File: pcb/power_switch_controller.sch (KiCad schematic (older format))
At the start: 38 parts, among them P1 PWR_JACK_2.5x5.5, P2 HEADER_01X03, P3 BNC_DOUBLE_RA, P4 HEADER_02X08, P5 HEADER_02X08, SW1 SPST_SERIES_M, U1 MAX6817, U2 TLE723X, U3 TLE723X

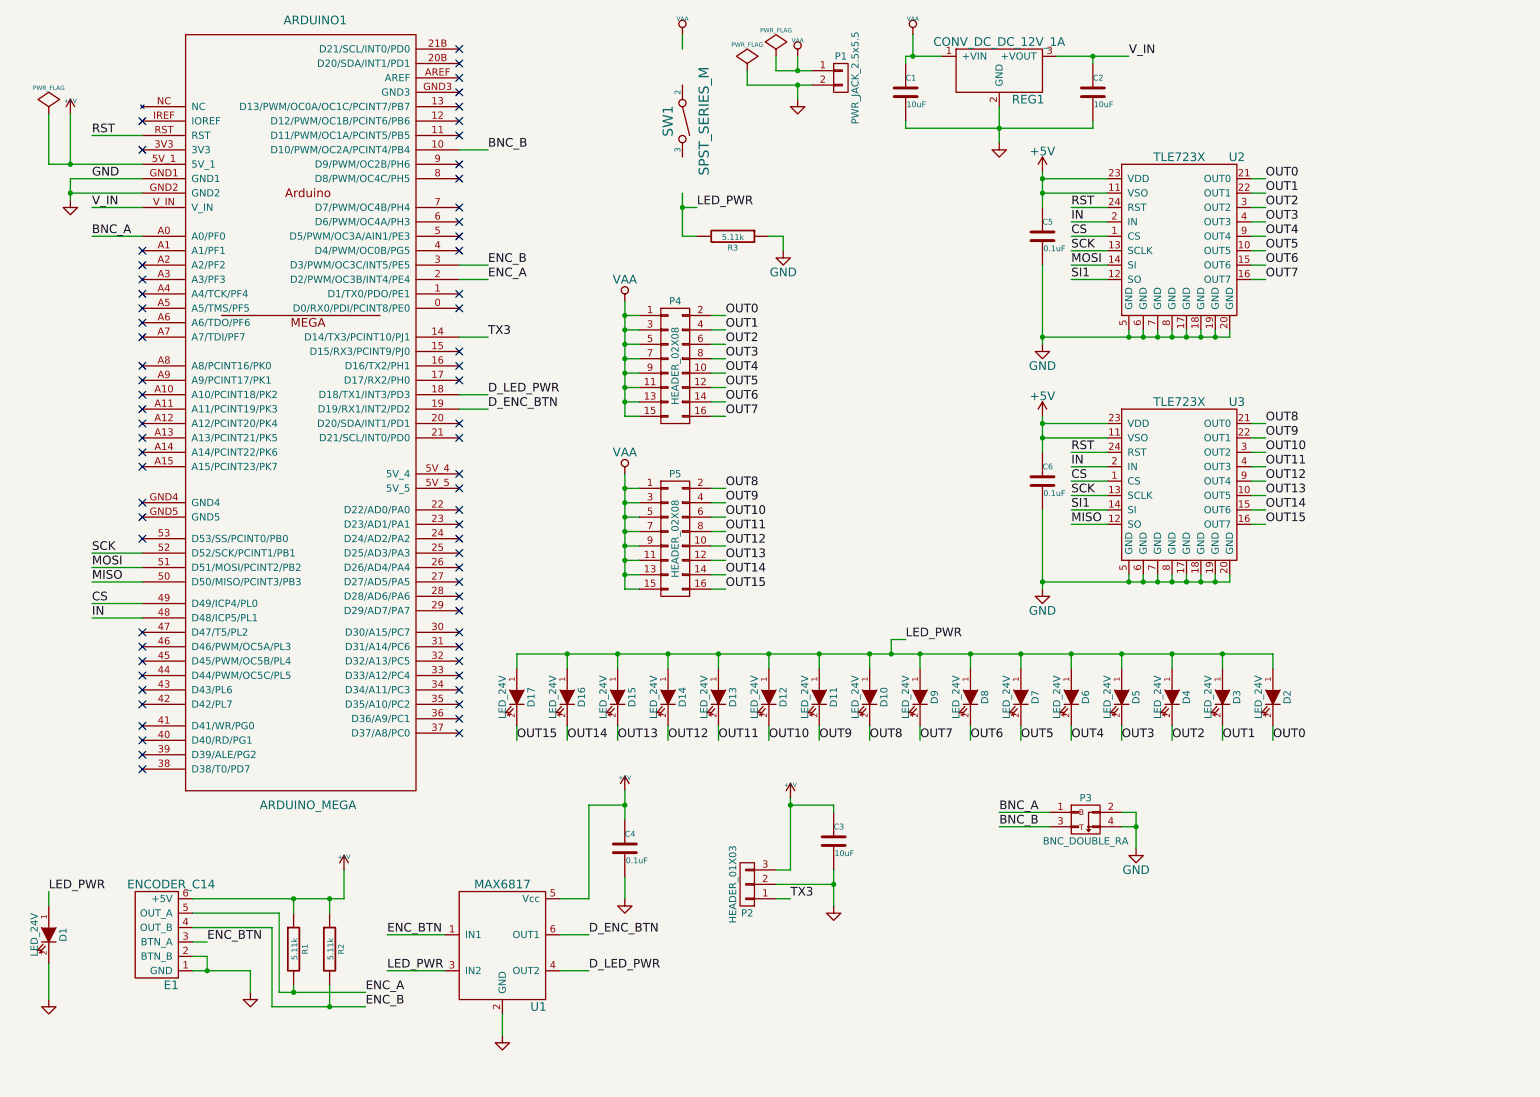
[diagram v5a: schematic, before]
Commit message: Progress towards 32 power switches.
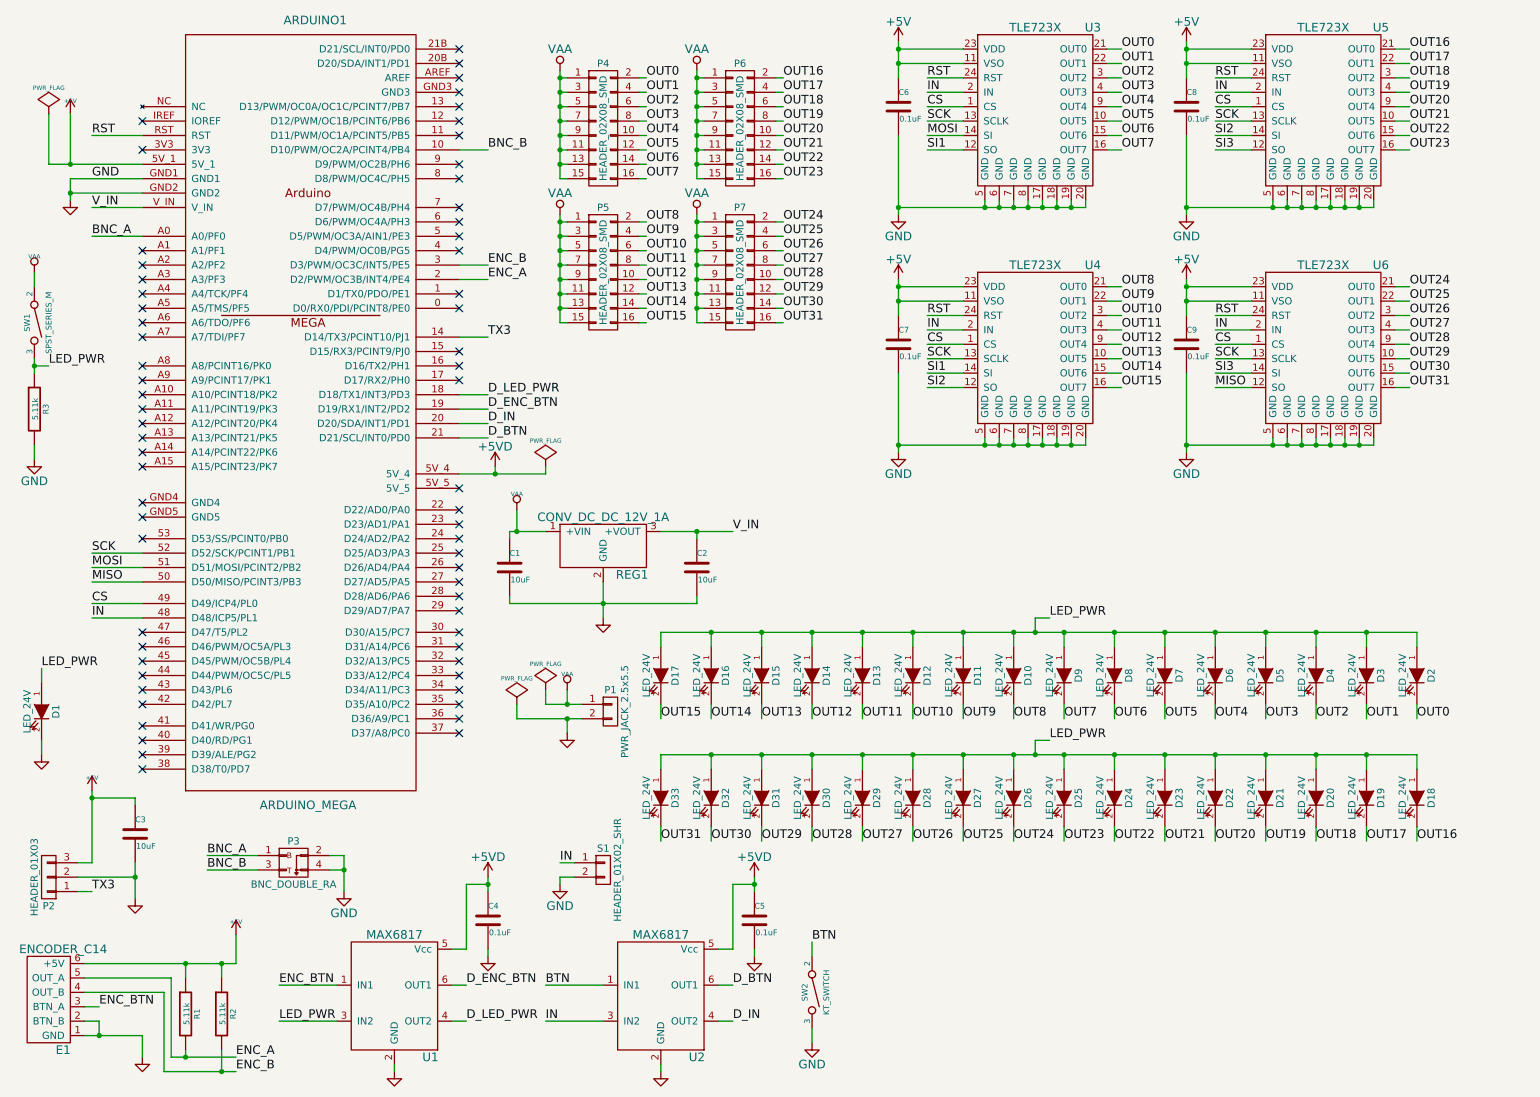
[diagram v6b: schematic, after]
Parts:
- removed P4, P5: HEADER_02X08, power_switch_controller:HEADER_02x08, symbol HEADER_02X08
- added C5, C6, C7: 0.1uF, power_switch_controller:SM1210, symbol 0.1uF
- added D10, D11, D12, D13, D14, D15, D16, D17, D2, D3, D4, D5, D6, D7, D8, D9: LED_24V, power_switch_controller:LED_555-3XXX, symbol LED_24V
- added P4, P5, P6, P7: HEADER_02X08_SMD, power_switch_controller:HEADER_02x08_SMD, symbol HEADER_02X08_SMD
- added S1: HEADER_01X02_SHR, power_switch_controller:Header_Shrouded_2_Pin, symbol HEADER_01X02_SHR
- added SW2: KT_SWITCH, power_switch_controller:KT_SWITCH, symbol KT_SWITCH
- added U2: MAX6817, power_switch_controller:MAX6817, symbol MAX6817
- added U3, U4: TLE723X, power_switch_controller:TLE723X, symbol TLE723X
- P2: footprint power_switch_controller:Header_Shrouded_3_Pin -> footprints:Header_3_Pin
- renumbered C5 to C8, C6 to C9, D2 to D18, D3 to D19, D4 to D20, D5 to D21, D6 to D22, D7 to D23, D8 to D24, D9 to D25, D10 to D26, D11 to D27, D12 to D28, D13 to D29, D14 to D30, D15 to D31, D16 to D32, D17 to D33, U2 to U5, U3 to U6
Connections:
- net +5V: now also C6.1, C7.1, U3.11 (VSO), U3.23 (VDD), U4.11 (VSO), U4.23 (VDD); no longer C4.1, U1.5 (Vcc)
- net CS: now also U3.1 (CS), U4.1 (CS)
- net GND: now also R3.2, C5.2, C6.2, C7.2, S1.2 (P2), SW2.3, U2.2 (GND), U3.17 (GND), U3.18 (GND), U3.19 (GND), U3.20 (GND), U3.5 (GND), U3.6 (GND), U3.7 (GND), U3.8 (GND), U4.17 (GND), U4.18 (GND), U4.19 (GND), U4.20 (GND), U4.5 (GND), U4.6 (GND), U4.7 (GND), U4.8 (GND); no longer R3.1
- net IN: now also S1.1 (P1), U2.3 (IN2), U3.2 (IN), U4.2 (IN)
- net LED_PWR: now also R3.1, SW1.3, D10.1 (A), D11.1 (A), D12.1 (A), D13.1 (A), D14.1 (A), D15.1 (A), D16.1 (A), D17.1 (A), D2.1 (A), D3.1 (A), D4.1 (A), D5.1 (A), D6.1 (A), D7.1 (A), D8.1 (A), D9.1 (A); no longer R3.2
- net MOSI: now also U3.14 (SI); no longer U5.14 (SI)
- net OUT0: now also D2.2 (K), P4.2 (P2), U3.21 (OUT0); no longer D18.2 (K), U5.21 (OUT0)
- net OUT1: now also D3.2 (K), P4.4 (P4), U3.22 (OUT1); no longer D19.2 (K), U5.22 (OUT1)
- net OUT10: now also D12.2 (K), P5.6 (P6), U4.3 (OUT2); no longer D28.2 (K), U6.3 (OUT2)
- net OUT11: now also D13.2 (K), P5.8 (P8), U4.4 (OUT3); no longer D29.2 (K), U6.4 (OUT3)
- net OUT12: now also D14.2 (K), P5.10 (P10), U4.9 (OUT4); no longer D30.2 (K), U6.9 (OUT4)
- net OUT13: now also D15.2 (K), P5.12 (P12), U4.10 (OUT5); no longer D31.2 (K), U6.10 (OUT5)
- net OUT14: now also D16.2 (K), P5.14 (P14), U4.15 (OUT6); no longer D32.2 (K), U6.15 (OUT6)
- net OUT15: now also D17.2 (K), P5.16 (P16), U4.16 (OUT7); no longer D33.2 (K), U6.16 (OUT7)
- net OUT2: now also D4.2 (K), P4.6 (P6), U3.3 (OUT2); no longer D20.2 (K), U5.3 (OUT2)
- net OUT3: now also D5.2 (K), P4.8 (P8), U3.4 (OUT3); no longer D21.2 (K), U5.4 (OUT3)
- net OUT4: now also D6.2 (K), P4.10 (P10), U3.9 (OUT4); no longer D22.2 (K), U5.9 (OUT4)
- net OUT5: now also D7.2 (K), P4.12 (P12), U3.10 (OUT5); no longer D23.2 (K), U5.10 (OUT5)
- net OUT6: now also D8.2 (K), P4.14 (P14), U3.15 (OUT6); no longer D24.2 (K), U5.15 (OUT6)
- net OUT7: now also D9.2 (K), P4.16 (P16), U3.16 (OUT7); no longer D25.2 (K), U5.16 (OUT7)
- net OUT8: now also D10.2 (K), P5.2 (P2), U4.21 (OUT0); no longer D26.2 (K), U6.21 (OUT0)
- net OUT9: now also D11.2 (K), P5.4 (P4), U4.22 (OUT1); no longer D27.2 (K), U6.22 (OUT1)
- net RST: now also U3.24 (RST), U4.24 (RST)
- net SCK: now also U3.13 (SCLK), U4.13 (SCLK)
- net SI1: now also U3.12 (SO), U4.14 (SI); no longer U5.12 (SO), U6.14 (SI)
- net VAA: now also SW1.2, P4.1 (P1), P4.11 (P11), P4.13 (P13), P4.15 (P15), P4.3 (P3), P4.5 (P5), P4.7 (P7), P4.9 (P9), P5.1 (P1), P5.11 (P11), P5.13 (P13), P5.15 (P15), P5.3 (P3), P5.5 (P5), P5.7 (P7), P5.9 (P9), P6.1 (P1), P6.11 (P11), P6.13 (P13), P6.15 (P15), P6.3 (P3), P6.5 (P5), P6.7 (P7), P6.9 (P9), P7.1 (P1), P7.11 (P11), P7.13 (P13), P7.15 (P15), P7.3 (P3), P7.5 (P5), P7.7 (P7), P7.9 (P9)
- net D_IN: now reaches ARDUINO1.20 (D20/SDA/INT1/PD1)
- net D_IN: now also U2.4 (OUT2)
- net D_BTN: now reaches ARDUINO1.21 (D21/SCL/INT0/PD0)
- net D_BTN: now also U2.6 (OUT1)
- net +5VD: now reaches ARDUINO1.5V_4
- net +5VD: now also C4.1, U1.5 (Vcc), C5.1, U2.5 (Vcc)
- new net BTN: SW2.2, U2.1 (IN1)
- new net OUT16: D18.2 (K), P6.2 (P2), U5.21 (OUT0)
- new net OUT17: D19.2 (K), P6.4 (P4), U5.22 (OUT1)
- new net OUT18: D20.2 (K), P6.6 (P6), U5.3 (OUT2)
- new net OUT19: D21.2 (K), P6.8 (P8), U5.4 (OUT3)
- new net OUT20: D22.2 (K), P6.10 (P10), U5.9 (OUT4)
- new net OUT21: D23.2 (K), P6.12 (P12), U5.10 (OUT5)
- new net OUT22: D24.2 (K), P6.14 (P14), U5.15 (OUT6)
- new net OUT23: D25.2 (K), P6.16 (P16), U5.16 (OUT7)
- new net OUT24: D26.2 (K), P7.2 (P2), U6.21 (OUT0)
- new net OUT25: D27.2 (K), P7.4 (P4), U6.22 (OUT1)
- new net OUT26: D28.2 (K), P7.6 (P6), U6.3 (OUT2)
- new net OUT27: D29.2 (K), P7.8 (P8), U6.4 (OUT3)
- new net OUT28: D30.2 (K), P7.10 (P10), U6.9 (OUT4)
- new net OUT29: D31.2 (K), P7.12 (P12), U6.10 (OUT5)
- new net OUT30: D32.2 (K), P7.14 (P14), U6.15 (OUT6)
- new net OUT31: D33.2 (K), P7.16 (P16), U6.16 (OUT7)
- new net SI2: U4.12 (SO), U5.14 (SI)
- new net SI3: U5.12 (SO), U6.14 (SI)
- no-connect marks 68 -> 65
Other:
- moved on the sheet: C1, C2, C3, C4, C8, C9, D1, D18, D19, D20, D21, D22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

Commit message: pcb v1.2.
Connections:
- net BNC_B: now also ARDUINO1.3 (D3/PWM/OC3C/INT5/PE5); no longer ARDUINO1.10 (D10/PWM/OC2A/PCINT4/PB4)
- net D_LED_PWR: now also ARDUINO1.17 (D17/RX2/PH0); no longer ARDUINO1.18 (D18/TX1/INT3/PD3)
- net ENC_A: now also ARDUINO1.18 (D18/TX1/INT3/PD3); no longer ARDUINO1.2 (D2/PWM/OC3B/INT4/PE4)
- net ENC_B: now also ARDUINO1.2 (D2/PWM/OC3B/INT4/PE4); no longer ARDUINO1.3 (D3/PWM/OC3C/INT5/PE5)
- net IN: no longer S1.1 (P1), U2.3 (IN2)
- net D_IN renamed D_SWITCH
- new net SWITCH: S1.1 (P1), U2.3 (IN2)
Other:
- moved on the sheet: P1
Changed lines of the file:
@@
 Title "power_switch_controller"
 Date ""
-Rev "1.1"
+Rev "1.2"
 Comp "Janelia"
 Comment1 ""
@@
 NoConn ~ 3550 2900
 NoConn ~ 3550 3000
-NoConn ~ 3550 3100
 NoConn ~ 3550 3850
 NoConn ~ 3550 4400
@@
 NoConn ~ 3550 4850
 NoConn ~ 3550 4950
-NoConn ~ 3550 5050
 NoConn ~ 3550 5150
 NoConn ~ 3550 5250
@@
 L GND #PWR04
 U 1 1 5474C6BF
-P 4300 5550
-F 0 "#PWR04" H 4300 5550 30  0001 C CNN
-F 1 "GND" H 4300 5480 30  0001 C CNN
-F 2 "" H 4300 5550 60  0000 C CNN
-F 3 "" H 4300 5550 60  0000 C CNN
-	1    4300 5550
+P 4250 5750
+F 0 "#PWR04" H 4250 5750 30  0001 C CNN
+F 1 "GND" H 4250 5680 30  0001 C CNN
+F 2 "" H 4250 5750 60  0000 C CNN
+F 3 "" H 4250 5750 60  0000 C CNN
+	1    4250 5750
 	1    0    0    -1
 $EndComp
@@
 L VAA #PWR05
 U 1 1 5474C6E7
-P 4300 5250
-F 0 "#PWR05" H 4300 5310 30  0001 C CNN
-F 1 "VAA" H 4300 5360 30  0000 C CNN
-F 2 "" H 4300 5250 60  0000 C CNN
-F 3 "" H 4300 5250 60  0000 C CNN
-	1    4300 5250
+P 4250 5450
+F 0 "#PWR05" H 4250 5510 30  0001 C CNN
+F 1 "VAA" H 4250 5560 30  0000 C CNN
+F 2 "" H 4250 5450 60  0000 C CNN
+F 3 "" H 4250 5450 60  0000 C CNN
+	1    4250 5450
 	1    0    0    -1
 $EndComp
@@
 L PWR_FLAG #FLG06
 U 1 1 5474C703
-P 4150 5250
-F 0 "#FLG06" H 4150 5345 30  0001 C CNN
-F 1 "PWR_FLAG" H 4150 5430 30  0000 C CNN
-F 2 "" H 4150 5250 60  0000 C CNN
-F 3 "" H 4150 5250 60  0000 C CNN
-	1    4150 5250
+P 4100 5450
+F 0 "#FLG06" H 4100 5545 30  0001 C CNN
+F 1 "PWR_FLAG" H 4100 5630 30  0000 C CNN
+F 2 "" H 4100 5450 60  0000 C CNN
+F 3 "" H 4100 5450 60  0000 C CNN
+	1    4100 5450
 	1    0    0    -1
 $EndComp
@@
 L PWR_FLAG #FLG07
 U 1 1 5474C71B
-P 3950 5350
-F 0 "#FLG07" H 3950 5445 30  0001 C CNN
-F 1 "PWR_FLAG" H 3950 5530 30  0000 C CNN
-F 2 "" H 3950 5350 60  0000 C CNN
-F 3 "" H 3950 5350 60  0000 C CNN
-	1    3950 5350
-	1    0    0    -1
-$EndComp
-Wire Wire Line
-	4150 5350 4400 5350
-Wire Wire Line
-	4150 5350 4150 5250
-Wire Wire Line
-	4300 5250 4300 5350
-Connection ~ 4300 5350
-Wire Wire Line
-	3950 5450 4400 5450
-Wire Wire Line
-	3950 5450 3950 5350
-Wire Wire Line
-	4300 5450 4300 5550
-Connection ~ 4300 5450
+P 3900 5550
+F 0 "#FLG07" H 3900 5645 30  0001 C CNN
+F 1 "PWR_FLAG" H 3900 5730 30  0000 C CNN
+F 2 "" H 3900 5550 60  0000 C CNN
+F 3 "" H 3900 5550 60  0000 C CNN
+	1    3900 5550
+	1    0    0    -1
+$EndComp
+Wire Wire Line
+	4100 5550 4350 5550
+Wire Wire Line
+	4100 5550 4100 5450
+Wire Wire Line
+	4250 5450 4250 5550
+Connection ~ 4250 5550
+Wire Wire Line
+	3900 5650 4350 5650
+Wire Wire Line
+	3900 5650 3900 5550
+Wire Wire Line
+	4250 5650 4250 5750
+Connection ~ 4250 5650
 Wire Wire Line
 	1350 1900 1000 1900
@@
 L PWR_JACK_2.5x5.5 P1
 U 1 1 5488FCDE
-P 4600 5400
-F 0 "P1" H 4600 5550 50  0000 C CNN
-F 1 "PWR_JACK_2.5x5.5" V 4700 5400 50  0000 C CNN
-F 2 "power_switch_controller:DCJACK_2PIN_HIGHCURRENT" H 4500 5450 60  0001 C CNN
-F 3 "" H 4600 5400 60  0000 C CNN
-F 4 "digikey" H 4700 5650 60  0001 C CNN "Vendor"
-F 5 "CP-063BH-ND" H 4800 5750 60  0001 C CNN "PartNumber"
-F 6 "CONN PWR JACK DC 2.5X5.5 8A T/H" H 4900 5850 60  0001 C CNN "Description"
-	1    4600 5400
+P 4550 5600
+F 0 "P1" H 4550 5750 50  0000 C CNN
+F 1 "PWR_JACK_2.5x5.5" V 4650 5600 50  0000 C CNN
+F 2 "power_switch_controller:DCJACK_2PIN_HIGHCURRENT" H 4450 5650 60  0001 C CNN
+F 3 "" H 4550 5600 60  0000 C CNN
+F 4 "digikey" H 4650 5850 60  0001 C CNN "Vendor"
+F 5 "CP-063BH-ND" H 4750 5950 60  0001 C CNN "PartNumber"
+F 6 "CONN PWR JACK DC 2.5X5.5 8A T/H" H 4850 6050 60  0001 C CNN "Description"
+	1    4550 5600
 	1    0    0    -1
 $EndComp
@@
 Text Label 3750 2800 0    60   ~ 0
 TX3
-Wire Wire Line
-	3550 2400 3750 2400
-Wire Wire Line
-	3550 2300 3750 2300
+Text Label 3750 3200 0    60   ~ 0
+ENC_A
 Text Label 3750 2400 0    60   ~ 0
-ENC_A
-Text Label 3750 2300 0    60   ~ 0
 ENC_B
 Wire Wire Line
@@
 Text Label 3600 7550 0    60   ~ 0
 D_LED_PWR
-Wire Wire Line
-	3550 3200 3750 3200
-Text Label 3750 3200 0    60   ~ 0
+Text Label 3750 3100 0    60   ~ 0
 D_LED_PWR
 $Comp
@@
 Text Label 1800 6500 0    60   ~ 0
 BNC_B
-Text Label 3750 1500 0    60   ~ 0
+Text Label 3750 2300 0    60   ~ 0
 BNC_B
 NoConn ~ 3550 1200
@@
 NoConn ~ 3550 900
 NoConn ~ 3550 800
-Wire Wire Line
-	3550 1500 3750 1500
 Wire Wire Line
 	4850 1000 4800 1000
@@
 	3550 3500 3750 3500
 Text Label 3750 3400 0    60   ~ 0
-D_IN
+D_SWITCH
 Text Label 3750 3500 0    60   ~ 0
 D_BTN
@@
 	4550 7550 4150 7550
 Text Label 4150 7550 0    60   ~ 0
-IN
+SWITCH
 Wire Wire Line
 	5350 7550 5450 7550
 Text Label 5450 7550 0    60   ~ 0
-D_IN
+D_SWITCH
 Wire Wire Line
 	5600 6550 5600 6650
@@
 $EndComp
 Wire Wire Line
-	4350 6450 4250 6450
-Text Label 4250 6450 0    60   ~ 0
-IN
+	4350 6450 4000 6450
+Text Label 4000 6450 0    60   ~ 0
+SWITCH
 $Comp
 L GND #PWR032
@@
 OUT15
 Wire Wire Line
-	4300 2700 4250 2700
-Wire Wire Line
-	4250 2700 4250 1950
+	4250 2700 4300 2700
+Wire Wire Line
+	4250 1950 4250 2700
 Wire Wire Line
 	4300 2000 4250 2000
@@
 Connection ~ 4250 2600
 Wire Wire Line
-	4300 1700 4250 1700
-Wire Wire Line
-	4250 1700 4250 950
+	4250 1700 4300 1700
+Wire Wire Line
+	4250 950  4250 1700
 Wire Wire Line
 	4300 1000 4250 1000
@@
 	5800 2700 5750 2700
 Wire Wire Line
-	5250 2700 5200 2700
-Wire Wire Line
-	5200 2700 5200 1950
+	5200 2700 5250 2700
+Wire Wire Line
+	5200 1950 5200 2700
 Wire Wire Line
 	5250 2000 5200 2000
@@
 Connection ~ 5200 2600
 Wire Wire Line
-	5250 1700 5200 1700
-Wire Wire Line
-	5200 1700 5200 950
+	5200 1700 5250 1700
+Wire Wire Line
+	5200 950  5200 1700
 Wire Wire Line
 	5250 1000 5200 1000
@@
 	1    0    0    -1
 $EndComp
+Wire Wire Line
+	3550 3200 3750 3200
+Wire Wire Line
+	3550 2400 3750 2400
+Wire Wire Line
+	3550 2300 3750 2300
+NoConn ~ 3550 1500
+NoConn ~ 3550 5050
+Wire Wire Line
+	3550 3100 3750 3100
 $EndSCHEMATC

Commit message: SPST switch -> DPST switch.
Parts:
- removed R3: 5.11k, power_switch_controller:SM1210, symbol 5.11k
- removed SW1: SPST_SERIES_M, power_switch_controller:SPST_SERIES_M, symbol SPST_SERIES_M
- added SW1: DPST_SERIES_M, power_switch_controller:DPST_SERIES_M, symbol DPST_SERIES_M
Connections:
- net GND: now also SW1.6
- net LED_PWR: now also SW1.3; no longer U1.3 (IN2)
- net VAA: now also SW1.2
- net D_LED_PWR renamed D_LIGHTS
- new net LIGHTS: SW1.5, U1.3 (IN2)
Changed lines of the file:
@@
 LIBS:memory
 LIBS:xilinx
-LIBS:special
 LIBS:microcontrollers
 LIBS:dsp
@@
 Title "power_switch_controller"
 Date ""
-Rev "1.2"
+Rev "1.3"
 Comp "Janelia"
 Comment1 ""
@@
 $EndComp
 $Comp
-L 5.11k R3
-U 1 1 54AD64AC
-P 600 3300
-F 0 "R3" V 680 3300 40  0000 C CNN
-F 1 "5.11k" V 607 3301 40  0000 C CNN
-F 2 "power_switch_controller:SM1210" V 530 3300 30  0001 C CNN
-F 3 "" H 600 3300 30  0000 C CNN
-F 4 "digikey" V 780 3400 60  0001 C CNN "Vendor"
-F 5 "P5.11KAACT-ND" V 880 3500 60  0001 C CNN "PartNumber"
-F 6 "RES SMD 5.11K OHM 1% 1/2W 1210" V 980 3600 60  0001 C CNN "Description"
-	1    600  3300
-	1    0    0    -1
-$EndComp
-$Comp
 L GND #PWR023
 U 1 1 54AD735F
-P 600 3650
-F 0 "#PWR023" H 600 3400 60  0001 C CNN
-F 1 "GND" H 600 3500 60  0000 C CNN
-F 2 "" H 600 3650 60  0000 C CNN
-F 3 "" H 600 3650 60  0000 C CNN
-	1    600  3650
+P 1000 3150
+F 0 "#PWR023" H 1000 2900 60  0001 C CNN
+F 1 "GND" H 1000 3000 60  0000 C CNN
+F 2 "" H 1000 3150 60  0000 C CNN
+F 3 "" H 1000 3150 60  0000 C CNN
+	1    1000 3150
 	1    0    0    -1
 $EndComp
@@
 	2700 7550 2300 7550
 Text Label 2300 7550 0    60   ~ 0
-LED_PWR
+LIGHTS
 Wire Wire Line
 	3500 7550 3600 7550
 Text Label 3600 7550 0    60   ~ 0
-D_LED_PWR
+D_LIGHTS
 Text Label 3750 3100 0    60   ~ 0
-D_LED_PWR
+D_LIGHTS
 $Comp
 L GND #PWR024
@@
 	3600 7050 3500 7050
 Connection ~ 3750 6600
-$Comp
-L SPST_SERIES_M SW1
-U 1 1 54BECF3D
-P 600 2700
-F 0 "SW1" H 600 2650 40  0000 C CNN
-F 1 "SPST_SERIES_M" H 600 2800 40  0000 C CNN
-F 2 "power_switch_controller:SPST_SERIES_M" H 500 2500 60  0001 C CNN
-F 3 "" H 600 2700 60  0000 C CNN
-F 4 "digikey" H 700 2900 60  0001 C CNN "Vendor"
-F 5 "360-3243-ND" H 800 3000 60  0001 C CNN "PartNumber"
-F 6 "SWITCH TOGGLE SPST 6A 125V" H 900 3100 60  0001 C CNN "Description"
-	1    600  2700
-	0    1    1    0
-$EndComp
 Wire Wire Line
 	600  2450 600  2350
-Wire Wire Line
-	600  2950 600  3050
-Wire Wire Line
-	600  3000 700  3000
-Connection ~ 600  3000
-Text Label 700  3000 0    60   ~ 0
+Text Label 600  3450 0    60   ~ 0
 LED_PWR
-Wire Wire Line
-	600  3550 600  3650
 $Comp
 L HEADER_01X03 P2
@@
 Wire Wire Line
 	3550 3100 3750 3100
+$Comp
+L DPST_SERIES_M SW1
+U 1 1 55C8F6FA
+P 800 2750
+F 0 "SW1" V 850 2800 50  0000 C CNN
+F 1 "DPST_SERIES_M" V 775 2775 30  0000 C CNN
+F 2 "power_switch_controller:DPST_SERIES_M" H 1000 2700 60  0001 C CNN
+F 3 "" H 1100 2800 60  0000 C CNN
+F 4 "digikey" H 1200 2900 60  0001 C CNN "Vendor"
+F 5 "360-3244-ND" H 1300 3000 60  0001 C CNN "PartNumber"
+F 6 "SWITCH TOGGLE DPST 6A 125V" H 1400 3100 60  0001 C CNN "Description"
+	1    800  2750
+	0    1    1    0
+$EndComp
+Wire Wire Line
+	1000 3050 1000 3150
+Wire Wire Line
+	1000 2450 1000 2350
+Text Label 1000 2350 0    60   ~ 0
+LIGHTS
+Wire Wire Line
+	600  3050 600  3450
 $EndSCHEMATC
